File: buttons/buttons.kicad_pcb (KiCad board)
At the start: 2 copper layers, 76 x 76 mm, 85 parts, among them J1 Conn_01x04, J2 USB_C_Receptacle_USB2.0, J3 Conn_01x03, SW1 SW_SPST, SW10 SW_SPST, SW11 SW_SPST, SW12 SW_SPST, SW13 SW_SPST, SW14 SW_SPST, SW15 SW_SPST, SW16 SW_SPST, SW17 SW_SPST, SW18 SW_SPST, SW2 SW_SPST, SW3 SW_SPST, SW4 SW_SPST, SW5 SW_SPST, SW6 SW_SPST, SW7 SW_SPST, SW8 SW_SPST, SW9 SW_SPST, U1 RP2040, U3 ip4234cz6, U4 AMS1117-3.3, Y1 12MHz

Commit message: Board ready for production
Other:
- board text added: "${COMPANY}"
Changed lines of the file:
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@@
     (date "2023-10-30")
     (rev "v0.3.1")
+    (company "Benjamin Crall")
   )
   (layers
@@
     (effects (font (size 0.8 0.8) (thickness 0.1)) (justify left bottom mirror))
   )
+  (gr_text "${COMPANY}" (at 150 125) (layer "B.SilkS")
+    (effects (font (size 1 1) (thickness 0.15)) (justify bottom mirror))
+  )
   (gr_text "JLCJLCJLCJLC" (at 184.7 73.95 90) (layer "F.SilkS")

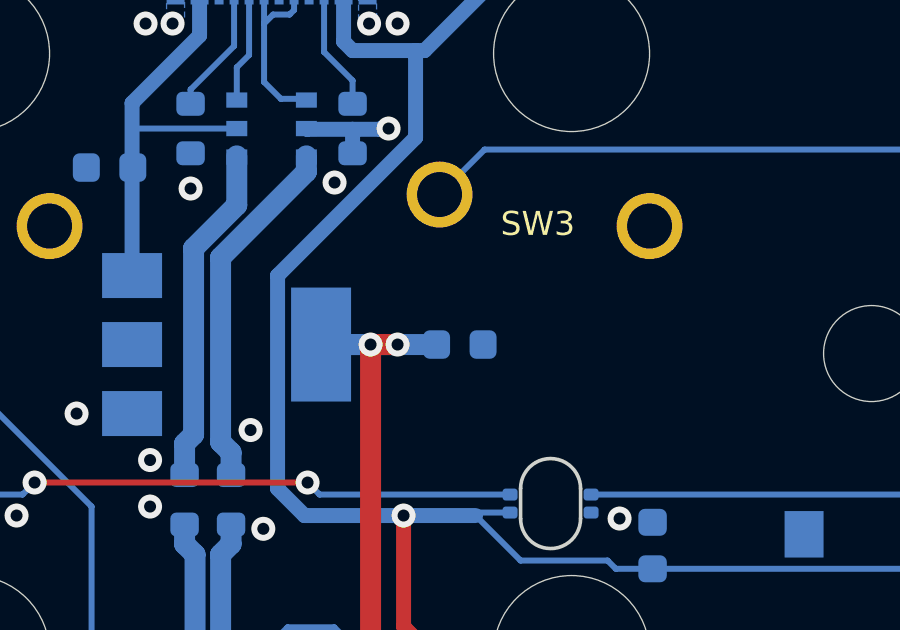
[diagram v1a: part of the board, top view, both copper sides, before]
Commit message: Added power LED
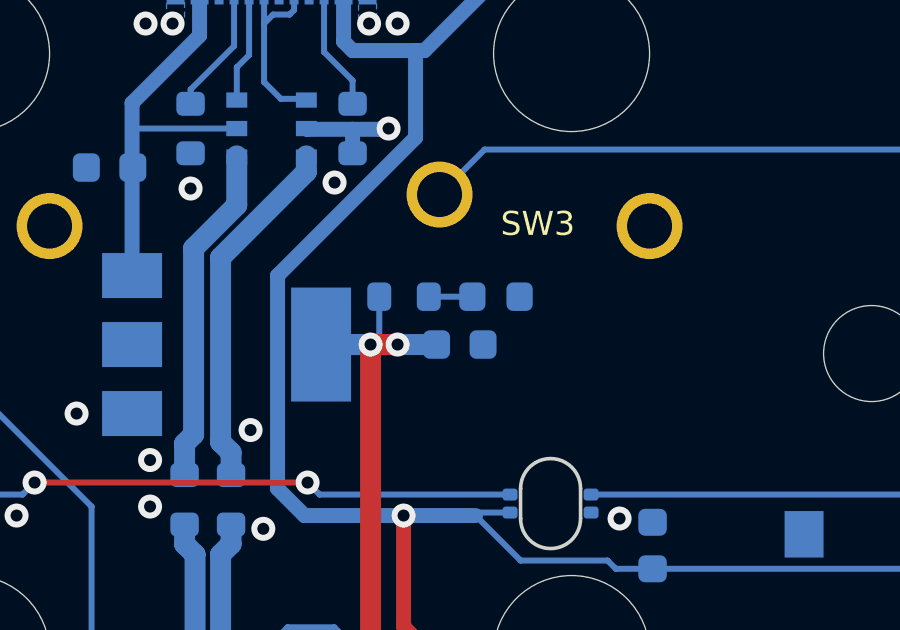
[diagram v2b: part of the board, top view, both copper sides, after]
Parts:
- added D18: LED_GREEN, LED_SMD:LED_0603_1608Metric, B.Cu at (157.5, 78.1)
- added R8: 470, Resistor_SMD:R_0603_1608Metric, B.Cu at (154.4, 78.1)
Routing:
- net +3V3: track 105.8 -> 107.6 mm
- net Net-(D18-A): track 0.00 -> 1.45 mm
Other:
- board text added: "3.3v"

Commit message: Picked components
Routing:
- net +5V: track 368.7 -> 360.5 mm
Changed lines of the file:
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@@
     (fp_line (start 4.47 2.48) (end 4.47 -4.84)
       (stroke (width 0.1) (type solid)) (layer "B.Fab"))
-    (pad "" np_thru_hole circle locked (at -2.89 1.45 180) (size 0.6 0.6) (drill 0.6) (layers "*.Cu" "*.Mask"))
-    (pad "" np_thru_hole circle locked (at 2.89 1.45 180) (size 0.6 0.6) (drill 0.6) (layers "*.Cu" "*.Mask"))
     (pad "A1" smd rect locked (at -3.2 2.51) (size 0.6 1.16) (layers "B.Cu" "B.Paste" "B.Mask")
       (net 3 "GND") (pinfunction "GND") (pintype "passive"))
@@
   (segment (start 135.725 107.25) (end 135.725 105.325) (width 0.2) (layer "B.Cu") (net 1))
   (segment (start 121.05 106.7) (end 122.575 108.225) (width 0.2) (layer "B.Cu") (net 1))
-  (segment (start 147.9 65.9) (end 144.8 65.9) (width 0.2) (layer "B.Cu") (net 1))
   (segment (start 120.73137 101.6) (end 125.33137 106.2) (width 1) (layer "B.Cu") (net 1))
   (segment (start 158.244814 127.05) (end 163.45 127.05) (width 0.2) (layer "B.Cu") (net 1))
@@
   (segment (start 157.95 126.75) (end 157.947407 126.752593) (width 0.2) (layer "B.Cu") (net 1))
   (segment (start 165 65.3) (end 175.2 65.3) (width 0.2) (layer "B.Cu") (net 1))
-  (segment (start 143.5 67.2) (end 142.6 67.2) (width 0.5) (layer "B.Cu") (net 1))
   (segment (start 163.225 67.075) (end 165 65.3) (width 0.2) (layer "B.Cu") (net 1))
   (segment (start 137.7 67) (end 121.384062 67) (width 0.5) (layer "B.Cu") (net 1))
-  (segment (start 147.6 67.785) (end 147.6 67.205) (width 0.2) (layer "B.Cu") (net 1))
   (segment (start 150.2 84.502082) (end 150.2 77.402082) (width 0.5) (layer "B.Cu") (net 1))
   (segment (start 117.15 85.75) (end 118.425 87.025) (width 0.2) (layer "B.Cu") (net 1))
   (segment (start 158.3 86.9) (end 161.2 86.9) (width 0.2) (layer "B.Cu") (net 1))
-  (segment (start 148.3 66.505) (end 148.3 66.3) (width 0.2) (layer "B.Cu") (net 1))
   (segment (start 117.5 66.8) (end 118 66.8) (width 0.5) (layer "B.Cu") (net 1))
   (segment (start 116.4 101.6) (end 120.73137 101.6) (width 1) (layer "B.Cu") (net 1))
@@
   (segment (start 162.7 107) (end 163.5 107) (width 0.2) (layer "B.Cu") (net 1))
   (segment (start 123.2 108.225) (end 123.2 108.8) (width 0.2) (layer "B.Cu") (net 1))
-  (segment (start 144.8 65.9) (end 144.3 66.4) (width 0.2) (layer "B.Cu") (net 1))
   (segment (start 121.384062 67) (end 121.184062 66.8) (width 0.5) (layer "B.Cu") (net 1))
   (segment (start 133 105.178681) (end 133 103.65) (width 1) (layer "B.Cu") (net 1))
@@
   (segment (start 113.1 104.9) (end 113.1 106.7) (width 0.2) (layer "B.Cu") (net 1))
   (segment (start 174.3 86.2) (end 175.225 86.2) (width 0.2) (layer "B.Cu") (net 1))
-  (segment (start 147.6 67.205) (end 148.3 66.505) (width 0.2) (layer "B.Cu") (net 1))
   (segment (start 158.702593 106.602593) (end 157.95 105.85) (width 0.2) (layer "B.Cu") (net 1))
   (segment (start 147.6 69.4) (end 145.35 71.65) (width 0.5) (layer "B.Cu") (net 1))
@@
   (segment (start 158.2 66.8) (end 157.95 66.55) (width 0.2) (layer "B.Cu") (net 1))
   (segment (start 113.1 104.9) (end 116.4 101.6) (width 1) (layer "B.Cu") (net 1))
-  (segment (start 144.3 66.4) (end 143.5 67.2) (width 0.5) (layer "B.Cu") (net 1))
   (segment (start 135.225 86.2) (end 135.225 85.325) (width 0.2) (layer "B.Cu") (net 1))
   (segment (start 163.5 107) (end 165.2 105.3) (width 0.2) (layer "B.Cu") (net 1))
@@
   (segment (start 137.9 66.8) (end 137.7 67) (width 0.5) (layer "B.Cu") (net 1))
   (segment (start 125.4 85.3) (end 135.2 85.3) (width 0.2) (layer "B.Cu") (net 1))
-  (segment (start 148.3 66.3) (end 147.9 65.9) (width 0.2) (layer "B.Cu") (net 1))
   (segment (start 121.459062 127.075) (end 121.136655 126.752593) (width 0.5) (layer "B.Cu") (net 1))
   (segment (start 151.097918 85.4) (end 150.2 84.502082) (width 0.5) (layer "B.Cu") (net 1))
@@
     (polygon
       (pts
-        (xy 143.2 62)
-        (xy 152.4 62)
-        (xy 152.4 66.9)
-        (xy 143.2 66.9)
+        (xy 142.946 62)
+        (xy 152.654 62)
+        (xy 152.654 67.535)
+        (xy 142.946 67.535)
       )
     )
@@
       )
     )
-  )
-  (zone (net 1) (net_name "+5V") (layer "B.Cu") (hatch edge 0.5)
-    (priority 3)
-    (connect_pads yes (clearance 0))
-    (min_thickness 0.2) (filled_areas_thickness no)
-    (fill yes (thermal_gap 0.5) (thermal_bridge_width 0.5))
-    (polygon
-      (pts
-        (xy 152.7 67.8)
-        (xy 152.7 67.1)
-        (xy 151.8 66.2)
-        (xy 148.2 66.2)
-        (xy 147.3 67.1)
-        (xy 147.3 67.8)
-      )
-    )
